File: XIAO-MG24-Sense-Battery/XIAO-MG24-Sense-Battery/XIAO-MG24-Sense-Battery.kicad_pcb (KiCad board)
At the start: 2 copper layers, 44.5 x 53 mm, 13 parts, among them J1 Conn_01x02_Pin, J2 Conn_01x02_Pin, J5 Conn_01x02_Pin, SW1 SS12D00G3, U1 XIAO-MG24-Sense

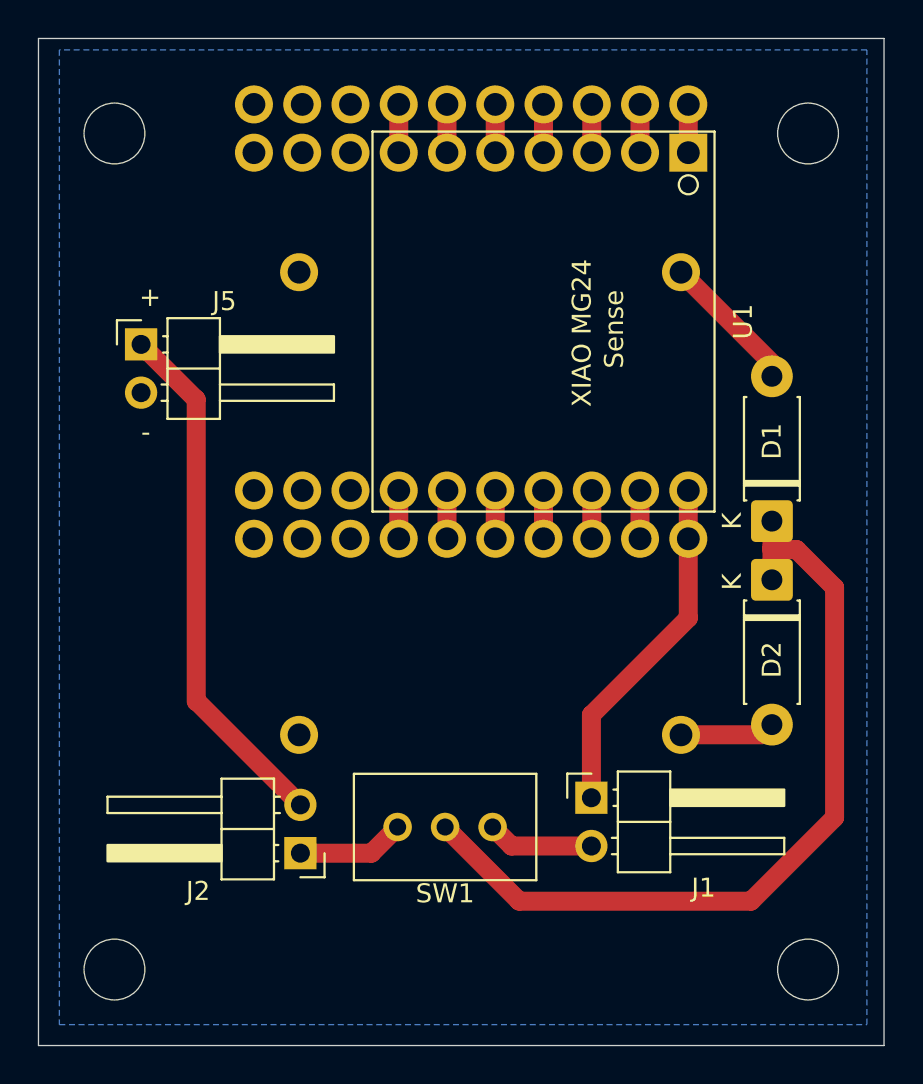
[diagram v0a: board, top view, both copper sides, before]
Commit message: Modified PCB Data
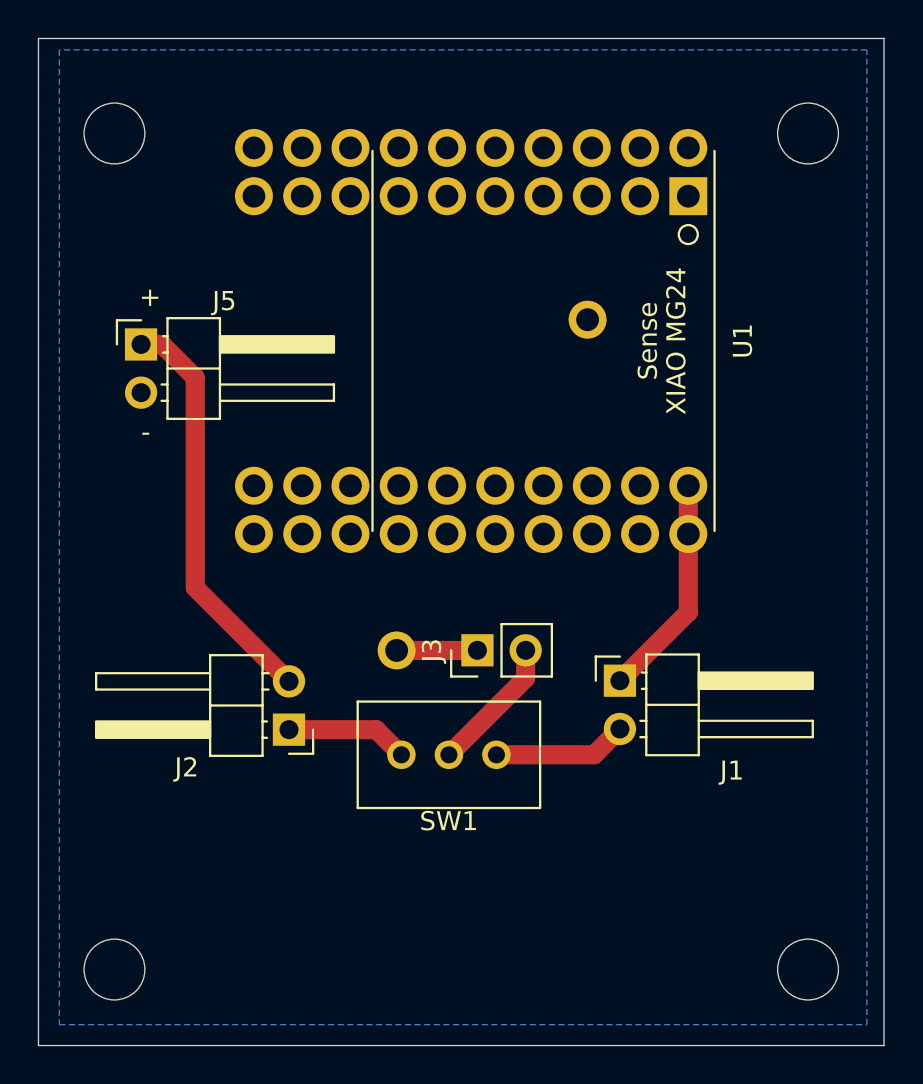
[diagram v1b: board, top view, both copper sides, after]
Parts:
- removed BT2: CR2032_Holder, CR2032-holder:CR2032-Holder
- removed D1, D2: D_Schottky, Diode_THT:D_DO-41_SOD81_P7.62mm_Horizontal
- added J3: Conn_01x02_Pin, Connector_PinHeader_2.54mm:PinHeader_1x02_P2.54mm_Vertical, F.Cu at (221.1, 57.2)
- moved BT1 11.2 mm to (221.8, 48.5), turned to 60 degrees
- moved J2 6.53 mm to (211.2, 61.4)
- moved J1 6.34 mm to (228.6, 58.8)
- moved SW1 3.81 mm to (222.1, 62.7)
- moved U1 1.02 mm to (224.6, 40.9)
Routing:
- net Net-(J3-Pin_2): track 43.3 -> 7.17 mm
- net 5V: track 18.3 -> 11.8 mm
- net Net-(J2-Pin_2): track 27.7 -> 21.6 mm
- net Net-(BT2-+): track 5.01 -> 0.00 mm
- net Net-(BT1-+): track 7.46 -> 4.25 mm
- net unconnected-(U1-D6/PC06/TX-Pad7)_1: track 2.54 -> 0.00 mm
- net unconnected-(U1-D5/PC05/SCL-Pad6)_1: track 2.54 -> 0.00 mm
- net unconnected-(U1-D4/PC04/SDA-Pad5): track 2.54 -> 0.00 mm
- net unconnected-(U1-D3/PB01-Pad4): track 2.54 -> 0.00 mm
- net unconnected-(U1-D2/PB00-Pad3): track 2.54 -> 0.00 mm
- net unconnected-(U1-D1/PA09-Pad2): track 2.54 -> 0.00 mm
- net unconnected-(U1-D0/PA08-Pad1)_1: track 2.54 -> 0.00 mm
- net unconnected-(U1-D9/PA04/MISO-Pad10): track 2.54 -> 0.00 mm
- net unconnected-(U1-D8/PA03/SCK-Pad9)_1: track 2.54 -> 0.00 mm
- net unconnected-(U1-D7/PC07/RX-Pad8): track 2.54 -> 0.00 mm
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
